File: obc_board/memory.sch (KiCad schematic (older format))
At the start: 10 parts

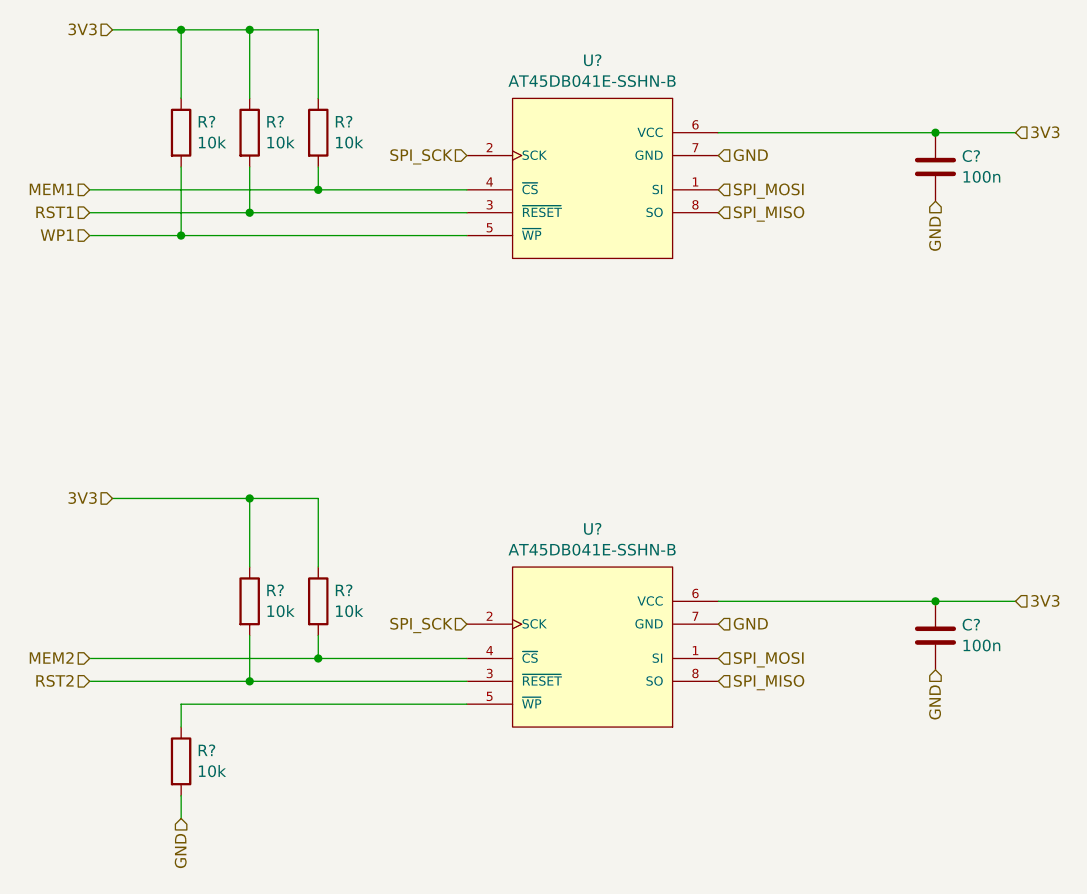
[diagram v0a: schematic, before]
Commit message: updated footprints
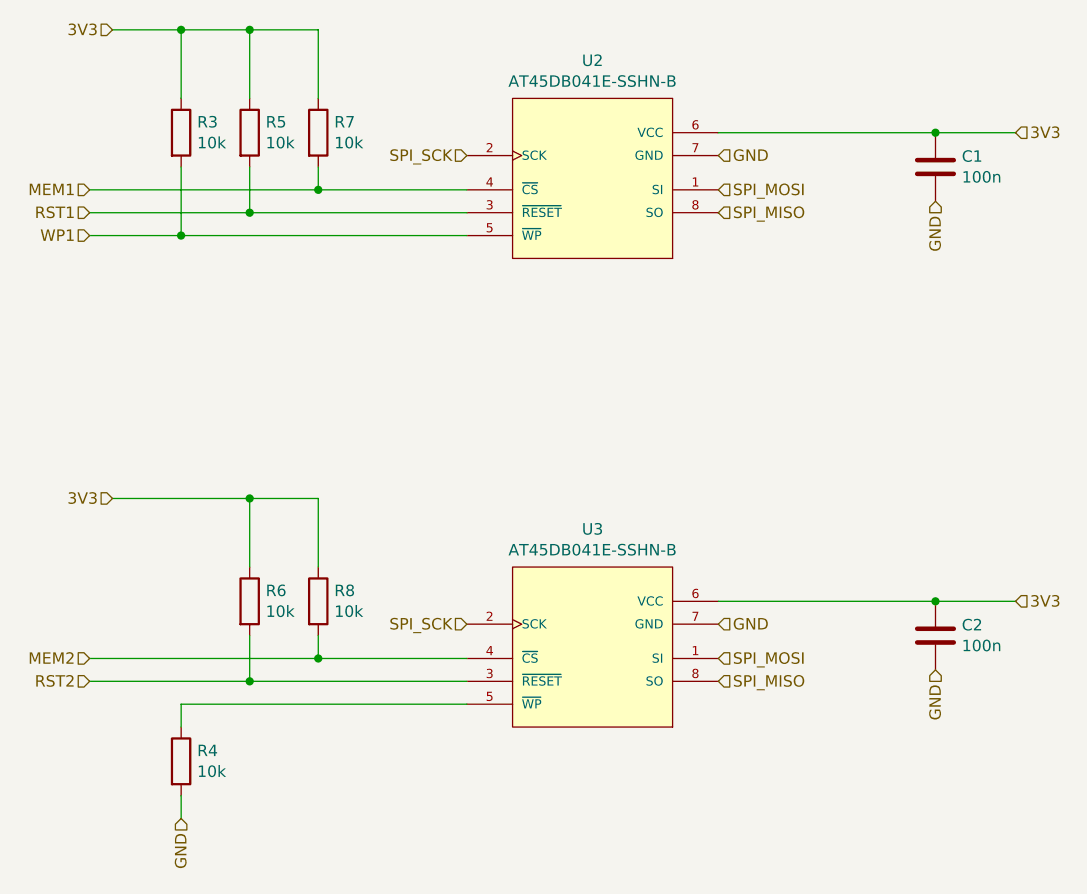
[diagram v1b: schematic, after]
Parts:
- C1, C2: renamed from C?; footprint (none) -> cubesat_obc:CAPC1005X55N; Digikey Part Number (none) -> 490-13342-1-ND
- U2, U3: renamed from U?; footprint SOIC127P600X175-8N -> Package_SO:SOIC-8-N7_3.9x4.9mm_P1.27mm; Digikey Part Number (none) -> 1265-1067-5-ND
- gave numbers to parts that had none: 6
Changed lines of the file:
@@
 P 5200 2950
 AR Path="/5E7EC636/5F3B7CBB" Ref="U?"  Part="1"
-AR Path="/5F3B62A5/5F3B7CBB" Ref="U?"  Part="1"
-F 0 "U?" H 5200 3765 50  0000 C CNN
+AR Path="/5F3B62A5/5F3B7CBB" Ref="U2"  Part="1"
+F 0 "U2" H 5200 3765 50  0000 C CNN
 F 1 "AT45DB041E-SSHN-B" H 5200 3674 50  0000 C CNN
-F 2 "SOIC127P600X175-8N" H 5200 2950 50  0001 L BNN
-F 3 "Adesto Technologies" H 5200 2950 50  0001 L BNN
+F 2 "Package_SO:SOIC-8-N7_3.9x4.9mm_P1.27mm" H 5200 2950 50  0001 L BNN
+F 3 "http://www.adestotech.com/wp-content/uploads/DS-AT45DB041E-HTADD.pdf" H 5200 2950 50  0001 L BNN
+F 4 "1265-1067-5-ND" H 5200 2950 50  0001 C CNN "Digikey Part Number"
 	1    5200 2950
 	1    0    0    -1
@@
 	5750 2450 6700 2450
 $Comp
-L Device:C C?
+L Device:C C1
 U 1 1 5F3B8BBB
 P 6700 2600
-F 0 "C?" H 6815 2646 50  0000 L CNN
+F 0 "C1" H 6815 2646 50  0000 L CNN
 F 1 "100n" H 6815 2555 50  0000 L CNN
-F 2 "" H 6738 2450 50  0001 C CNN
-F 3 "~" H 6700 2600 50  0001 C CNN
+F 2 "cubesat_obc:CAPC1005X55N" H 6738 2450 50  0001 C CNN
+F 3 "https://search.murata.co.jp/Ceramy/image/img/A01X/G101/ENG/GRM155R71H104KE14-01.pdf" H 6700 2600 50  0001 C CNN
+F 4 "	490-13342-1-ND" H 6700 2600 50  0001 C CNN "Digikey Part Number"
 	1    6700 2600
 	1    0    0    -1
@@
 RST1
 $Comp
-L Device:R R?
+L Device:R R7
 U 1 1 5F42F3C4
 P 4000 2450
-F 0 "R?" H 4070 2496 50  0000 L CNN
+F 0 "R7" H 4070 2496 50  0000 L CNN
 F 1 "10k" H 4070 2405 50  0000 L CNN
 F 2 "" V 3930 2450 50  0001 C CNN
@@
 	4000 2700 4650 2700
 $Comp
-L Device:R R?
+L Device:R R5
 U 1 1 5F4303A6
 P 3700 2450
-F 0 "R?" H 3770 2496 50  0000 L CNN
+F 0 "R5" H 3770 2496 50  0000 L CNN
 F 1 "10k" H 3770 2405 50  0000 L CNN
 F 2 "" V 3630 2450 50  0001 C CNN
@@
 $EndComp
 $Comp
-L Device:R R?
+L Device:R R3
 U 1 1 5F430694
 P 3400 2450
-F 0 "R?" H 3470 2496 50  0000 L CNN
+F 0 "R3" H 3470 2496 50  0000 L CNN
 F 1 "10k" H 3470 2405 50  0000 L CNN
 F 2 "" V 3330 2450 50  0001 C CNN
@@
 P 5200 5000
 AR Path="/5E7EC636/5F434A8C" Ref="U?"  Part="1"
-AR Path="/5F3B62A5/5F434A8C" Ref="U?"  Part="1"
-F 0 "U?" H 5200 5815 50  0000 C CNN
+AR Path="/5F3B62A5/5F434A8C" Ref="U3"  Part="1"
+F 0 "U3" H 5200 5815 50  0000 C CNN
 F 1 "AT45DB041E-SSHN-B" H 5200 5724 50  0000 C CNN
-F 2 "SOIC127P600X175-8N" H 5200 5000 50  0001 L BNN
-F 3 "Adesto Technologies" H 5200 5000 50  0001 L BNN
+F 2 "Package_SO:SOIC-8-N7_3.9x4.9mm_P1.27mm" H 5200 5000 50  0001 L BNN
+F 3 "http://www.adestotech.com/wp-content/uploads/DS-AT45DB041E-HTADD.pdf" H 5200 5000 50  0001 L BNN
+F 4 "1265-1067-5-ND" H 5200 5000 50  0001 C CNN "Digikey Part Number"
 	1    5200 5000
 	1    0    0    -1
@@
 	5750 4500 6700 4500
 $Comp
-L Device:C C?
+L Device:C C2
 U 1 1 5F434A98
 P 6700 4650
-F 0 "C?" H 6815 4696 50  0000 L CNN
+F 0 "C2" H 6815 4696 50  0000 L CNN
 F 1 "100n" H 6815 4605 50  0000 L CNN
-F 2 "" H 6738 4500 50  0001 C CNN
-F 3 "~" H 6700 4650 50  0001 C CNN
+F 2 "cubesat_obc:CAPC1005X55N" H 6738 4500 50  0001 C CNN
+F 3 "https://search.murata.co.jp/Ceramy/image/img/A01X/G101/ENG/GRM155R71H104KE14-01.pdf" H 6700 4650 50  0001 C CNN
+F 4 "	490-13342-1-ND" H 6700 4650 50  0001 C CNN "Digikey Part Number"
 	1    6700 4650
 	1    0    0    -1
@@
 RST2
 $Comp
-L Device:R R?
+L Device:R R8
 U 1 1 5F434AA3
 P 4000 4500
-F 0 "R?" H 4070 4546 50  0000 L CNN
+F 0 "R8" H 4070 4546 50  0000 L CNN
 F 1 "10k" H 4070 4455 50  0000 L CNN
 F 2 "" V 3930 4500 50  0001 C CNN
@@
 	4000 4750 4650 4750
 $Comp
-L Device:R R?
+L Device:R R6
 U 1 1 5F434AAD
 P 3700 4500
-F 0 "R?" H 3770 4546 50  0000 L CNN
+F 0 "R6" H 3770 4546 50  0000 L CNN
 F 1 "10k" H 3770 4455 50  0000 L CNN
 F 2 "" V 3630 4500 50  0001 C CNN
@@
 Connection ~ 3400 2900
 $Comp
-L Device:R R?
+L Device:R R4
 U 1 1 5F43582E
 P 3400 5200
-F 0 "R?" H 3470 5246 50  0000 L CNN
+F 0 "R4" H 3470 5246 50  0000 L CNN
 F 1 "10k" H 3470 5155 50  0000 L CNN
 F 2 "" V 3330 5200 50  0001 C CNN

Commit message: footprints
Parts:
- C1, C2: footprint cubesat_obc:CAPC1005X55N -> Capacitor_SMD:C_0402_1005Metric; Digikey Part Number 490-13342-1-ND -> 490-16433-1-ND
- R3, R4, R5, R6, R7, R8: footprint (none) -> Resistor_SMD:R_0402_1005Metric; Digikey Part Number (none) -> 311-10.0KLRCT-ND
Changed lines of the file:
@@
 F 0 "C1" H 6815 2646 50  0000 L CNN
 F 1 "100n" H 6815 2555 50  0000 L CNN
-F 2 "cubesat_obc:CAPC1005X55N" H 6738 2450 50  0001 C CNN
-F 3 "https://search.murata.co.jp/Ceramy/image/img/A01X/G101/ENG/GRM155R71H104KE14-01.pdf" H 6700 2600 50  0001 C CNN
-F 4 "	490-13342-1-ND" H 6700 2600 50  0001 C CNN "Digikey Part Number"
+F 2 "Capacitor_SMD:C_0402_1005Metric" H 6738 2450 50  0001 C CNN
+F 3 "https://search.murata.co.jp/Ceramy/image/img/A01X/G101/ENG/GCM155R71C104JA55-01.pdf" H 6700 2600 50  0001 C CNN
+F 4 "490-16433-1-ND" H 6700 2600 50  0001 C CNN "Digikey Part Number"
 	1    6700 2600
 	1    0    0    -1
@@
 F 0 "R7" H 4070 2496 50  0000 L CNN
 F 1 "10k" H 4070 2405 50  0000 L CNN
-F 2 "" V 3930 2450 50  0001 C CNN
-F 3 "~" H 4000 2450 50  0001 C CNN
+F 2 "Resistor_SMD:R_0402_1005Metric" V 3930 2450 50  0001 C CNN
+F 3 "https://www.yageo.com/upload/media/product/productsearch/datasheet/rchip/PYu-RC_Group_51_RoHS_L_11.pdf~" H 4000 2450 50  0001 C CNN
+F 4 "311-10.0KLRCT-ND" H 4000 2450 50  0001 C CNN "Digikey Part Number"
 	1    4000 2450
 	1    0    0    -1
@@
 F 0 "R5" H 3770 2496 50  0000 L CNN
 F 1 "10k" H 3770 2405 50  0000 L CNN
-F 2 "" V 3630 2450 50  0001 C CNN
-F 3 "~" H 3700 2450 50  0001 C CNN
+F 2 "Resistor_SMD:R_0402_1005Metric" V 3630 2450 50  0001 C CNN
+F 3 "https://www.yageo.com/upload/media/product/productsearch/datasheet/rchip/PYu-RC_Group_51_RoHS_L_11.pdf~" H 3700 2450 50  0001 C CNN
+F 4 "311-10.0KLRCT-ND" H 3700 2450 50  0001 C CNN "Digikey Part Number"
 	1    3700 2450
 	1    0    0    -1
@@
 F 0 "R3" H 3470 2496 50  0000 L CNN
 F 1 "10k" H 3470 2405 50  0000 L CNN
-F 2 "" V 3330 2450 50  0001 C CNN
-F 3 "~" H 3400 2450 50  0001 C CNN
+F 2 "Resistor_SMD:R_0402_1005Metric" V 3330 2450 50  0001 C CNN
+F 3 "https://www.yageo.com/upload/media/product/productsearch/datasheet/rchip/PYu-RC_Group_51_RoHS_L_11.pdf~" H 3400 2450 50  0001 C CNN
+F 4 "311-10.0KLRCT-ND" H 3400 2450 50  0001 C CNN "Digikey Part Number"
 	1    3400 2450
 	1    0    0    -1
@@
 F 0 "C2" H 6815 4696 50  0000 L CNN
 F 1 "100n" H 6815 4605 50  0000 L CNN
-F 2 "cubesat_obc:CAPC1005X55N" H 6738 4500 50  0001 C CNN
-F 3 "https://search.murata.co.jp/Ceramy/image/img/A01X/G101/ENG/GRM155R71H104KE14-01.pdf" H 6700 4650 50  0001 C CNN
-F 4 "	490-13342-1-ND" H 6700 4650 50  0001 C CNN "Digikey Part Number"
+F 2 "Capacitor_SMD:C_0402_1005Metric" H 6738 4500 50  0001 C CNN
+F 3 "https://search.murata.co.jp/Ceramy/image/img/A01X/G101/ENG/GCM155R71C104JA55-01.pdf" H 6700 4650 50  0001 C CNN
+F 4 "490-16433-1-ND" H 6700 4650 50  0001 C CNN "Digikey Part Number"
 	1    6700 4650
 	1    0    0    -1
@@
 F 0 "R8" H 4070 4546 50  0000 L CNN
 F 1 "10k" H 4070 4455 50  0000 L CNN
-F 2 "" V 3930 4500 50  0001 C CNN
-F 3 "~" H 4000 4500 50  0001 C CNN
+F 2 "Resistor_SMD:R_0402_1005Metric" V 3930 4500 50  0001 C CNN
+F 3 "https://www.yageo.com/upload/media/product/productsearch/datasheet/rchip/PYu-RC_Group_51_RoHS_L_11.pdf~" H 4000 4500 50  0001 C CNN
+F 4 "311-10.0KLRCT-ND" H 4000 4500 50  0001 C CNN "Digikey Part Number"
 	1    4000 4500
 	1    0    0    -1
@@
 F 0 "R6" H 3770 4546 50  0000 L CNN
 F 1 "10k" H 3770 4455 50  0000 L CNN
-F 2 "" V 3630 4500 50  0001 C CNN
-F 3 "~" H 3700 4500 50  0001 C CNN
+F 2 "Resistor_SMD:R_0402_1005Metric" V 3630 4500 50  0001 C CNN
+F 3 "https://www.yageo.com/upload/media/product/productsearch/datasheet/rchip/PYu-RC_Group_51_RoHS_L_11.pdf~" H 3700 4500 50  0001 C CNN
+F 4 "311-10.0KLRCT-ND" H 3700 4500 50  0001 C CNN "Digikey Part Number"
 	1    3700 4500
 	1    0    0    -1
@@
 F 0 "R4" H 3470 5246 50  0000 L CNN
 F 1 "10k" H 3470 5155 50  0000 L CNN
-F 2 "" V 3330 5200 50  0001 C CNN
-F 3 "~" H 3400 5200 50  0001 C CNN
+F 2 "Resistor_SMD:R_0402_1005Metric" V 3330 5200 50  0001 C CNN
+F 3 "https://www.yageo.com/upload/media/product/productsearch/datasheet/rchip/PYu-RC_Group_51_RoHS_L_11.pdf~" H 3400 5200 50  0001 C CNN
+F 4 "311-10.0KLRCT-ND" H 3400 5200 50  0001 C CNN "Digikey Part Number"
 	1    3400 5200
 	1    0    0    -1

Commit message: expose more ios
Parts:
- U2, U3: footprint Package_SO:SOIC-8-N7_3.9x4.9mm_P1.27mm -> Package_SO:SOIC-8_3.9x4.9mm_P1.27mm
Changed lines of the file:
@@
 $Descr A4 11693 8268
 encoding utf-8
-Sheet 2 5
+Sheet 2 6
 Title ""
 Date ""
@@
 F 0 "U2" H 5200 3765 50  0000 C CNN
 F 1 "AT45DB041E-SSHN-B" H 5200 3674 50  0000 C CNN
-F 2 "Package_SO:SOIC-8-N7_3.9x4.9mm_P1.27mm" H 5200 2950 50  0001 L BNN
+F 2 "Package_SO:SOIC-8_3.9x4.9mm_P1.27mm" H 5200 2950 50  0001 L BNN
 F 3 "http://www.adestotech.com/wp-content/uploads/DS-AT45DB041E-HTADD.pdf" H 5200 2950 50  0001 L BNN
 F 4 "1265-1067-5-ND" H 5200 2950 50  0001 C CNN "Digikey Part Number"
@@
 F 0 "U3" H 5200 5815 50  0000 C CNN
 F 1 "AT45DB041E-SSHN-B" H 5200 5724 50  0000 C CNN
-F 2 "Package_SO:SOIC-8-N7_3.9x4.9mm_P1.27mm" H 5200 5000 50  0001 L BNN
+F 2 "Package_SO:SOIC-8_3.9x4.9mm_P1.27mm" H 5200 5000 50  0001 L BNN
 F 3 "http://www.adestotech.com/wp-content/uploads/DS-AT45DB041E-HTADD.pdf" H 5200 5000 50  0001 L BNN
 F 4 "1265-1067-5-ND" H 5200 5000 50  0001 C CNN "Digikey Part Number"

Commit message: pcb layout
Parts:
- renumbered U2 to U1, U3 to U2
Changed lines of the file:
@@
 $Descr A4 11693 8268
 encoding utf-8
-Sheet 2 6
+Sheet 2 7
 Title ""
 Date ""
@@
 P 5200 2950
 AR Path="/5E7EC636/5F3B7CBB" Ref="U?"  Part="1"
-AR Path="/5F3B62A5/5F3B7CBB" Ref="U2"  Part="1"
-F 0 "U2" H 5200 3765 50  0000 C CNN
+AR Path="/5F3B62A5/5F3B7CBB" Ref="U1"  Part="1"
+F 0 "U1" H 5200 3765 50  0000 C CNN
 F 1 "AT45DB041E-SSHN-B" H 5200 3674 50  0000 C CNN
 F 2 "Package_SO:SOIC-8_3.9x4.9mm_P1.27mm" H 5200 2950 50  0001 L BNN
@@
 F 1 "10k" H 4070 2405 50  0000 L CNN
 F 2 "Resistor_SMD:R_0402_1005Metric" V 3930 2450 50  0001 C CNN
-F 3 "https://www.yageo.com/upload/media/product/productsearch/datasheet/rchip/PYu-RC_Group_51_RoHS_L_11.pdf~" H 4000 2450 50  0001 C CNN
+F 3 "https://www.yageo.com/upload/media/product/productsearch/datasheet/rchip/PYu-RC_Group_51_RoHS_L_11.pdf" H 4000 2450 50  0001 C CNN
 F 4 "311-10.0KLRCT-ND" H 4000 2450 50  0001 C CNN "Digikey Part Number"
 	1    4000 2450
@@
 F 1 "10k" H 3770 2405 50  0000 L CNN
 F 2 "Resistor_SMD:R_0402_1005Metric" V 3630 2450 50  0001 C CNN
-F 3 "https://www.yageo.com/upload/media/product/productsearch/datasheet/rchip/PYu-RC_Group_51_RoHS_L_11.pdf~" H 3700 2450 50  0001 C CNN
+F 3 "https://www.yageo.com/upload/media/product/productsearch/datasheet/rchip/PYu-RC_Group_51_RoHS_L_11.pdf" H 3700 2450 50  0001 C CNN
 F 4 "311-10.0KLRCT-ND" H 3700 2450 50  0001 C CNN "Digikey Part Number"
 	1    3700 2450
@@
 F 1 "10k" H 3470 2405 50  0000 L CNN
 F 2 "Resistor_SMD:R_0402_1005Metric" V 3330 2450 50  0001 C CNN
-F 3 "https://www.yageo.com/upload/media/product/productsearch/datasheet/rchip/PYu-RC_Group_51_RoHS_L_11.pdf~" H 3400 2450 50  0001 C CNN
+F 3 "https://www.yageo.com/upload/media/product/productsearch/datasheet/rchip/PYu-RC_Group_51_RoHS_L_11.pdf" H 3400 2450 50  0001 C CNN
 F 4 "311-10.0KLRCT-ND" H 3400 2450 50  0001 C CNN "Digikey Part Number"
 	1    3400 2450
@@
 P 5200 5000
 AR Path="/5E7EC636/5F434A8C" Ref="U?"  Part="1"
-AR Path="/5F3B62A5/5F434A8C" Ref="U3"  Part="1"
-F 0 "U3" H 5200 5815 50  0000 C CNN
+AR Path="/5F3B62A5/5F434A8C" Ref="U2"  Part="1"
+F 0 "U2" H 5200 5815 50  0000 C CNN
 F 1 "AT45DB041E-SSHN-B" H 5200 5724 50  0000 C CNN
 F 2 "Package_SO:SOIC-8_3.9x4.9mm_P1.27mm" H 5200 5000 50  0001 L BNN
@@
 F 1 "10k" H 4070 4455 50  0000 L CNN
 F 2 "Resistor_SMD:R_0402_1005Metric" V 3930 4500 50  0001 C CNN
-F 3 "https://www.yageo.com/upload/media/product/productsearch/datasheet/rchip/PYu-RC_Group_51_RoHS_L_11.pdf~" H 4000 4500 50  0001 C CNN
+F 3 "https://www.yageo.com/upload/media/product/productsearch/datasheet/rchip/PYu-RC_Group_51_RoHS_L_11.pdf" H 4000 4500 50  0001 C CNN
 F 4 "311-10.0KLRCT-ND" H 4000 4500 50  0001 C CNN "Digikey Part Number"
 	1    4000 4500
@@
 F 1 "10k" H 3770 4455 50  0000 L CNN
 F 2 "Resistor_SMD:R_0402_1005Metric" V 3630 4500 50  0001 C CNN
-F 3 "https://www.yageo.com/upload/media/product/productsearch/datasheet/rchip/PYu-RC_Group_51_RoHS_L_11.pdf~" H 3700 4500 50  0001 C CNN
+F 3 "https://www.yageo.com/upload/media/product/productsearch/datasheet/rchip/PYu-RC_Group_51_RoHS_L_11.pdf" H 3700 4500 50  0001 C CNN
 F 4 "311-10.0KLRCT-ND" H 3700 4500 50  0001 C CNN "Digikey Part Number"
 	1    3700 4500
@@
 F 1 "10k" H 3470 5155 50  0000 L CNN
 F 2 "Resistor_SMD:R_0402_1005Metric" V 3330 5200 50  0001 C CNN
-F 3 "https://www.yageo.com/upload/media/product/productsearch/datasheet/rchip/PYu-RC_Group_51_RoHS_L_11.pdf~" H 3400 5200 50  0001 C CNN
+F 3 "https://www.yageo.com/upload/media/product/productsearch/datasheet/rchip/PYu-RC_Group_51_RoHS_L_11.pdf" H 3400 5200 50  0001 C CNN
 F 4 "311-10.0KLRCT-ND" H 3400 5200 50  0001 C CNN "Digikey Part Number"
 	1    3400 5200

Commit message: relayout
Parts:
- renumbered C1 to C19, C2 to C20, U1 to U2, U2 to U3
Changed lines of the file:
@@
 P 5200 2950
 AR Path="/5E7EC636/5F3B7CBB" Ref="U?"  Part="1"
-AR Path="/5F3B62A5/5F3B7CBB" Ref="U1"  Part="1"
-F 0 "U1" H 5200 3765 50  0000 C CNN
+AR Path="/5F3B62A5/5F3B7CBB" Ref="U2"  Part="1"
+F 0 "U2" H 5200 3765 50  0000 C CNN
 F 1 "AT45DB041E-SSHN-B" H 5200 3674 50  0000 C CNN
 F 2 "Package_SO:SOIC-8_3.9x4.9mm_P1.27mm" H 5200 2950 50  0001 L BNN
@@
 	5750 2450 6700 2450
 $Comp
-L Device:C C1
+L Device:C C19
 U 1 1 5F3B8BBB
 P 6700 2600
-F 0 "C1" H 6815 2646 50  0000 L CNN
+F 0 "C19" H 6815 2646 50  0000 L CNN
 F 1 "100n" H 6815 2555 50  0000 L CNN
 F 2 "Capacitor_SMD:C_0402_1005Metric" H 6738 2450 50  0001 C CNN
@@
 P 5200 5000
 AR Path="/5E7EC636/5F434A8C" Ref="U?"  Part="1"
-AR Path="/5F3B62A5/5F434A8C" Ref="U2"  Part="1"
-F 0 "U2" H 5200 5815 50  0000 C CNN
+AR Path="/5F3B62A5/5F434A8C" Ref="U3"  Part="1"
+F 0 "U3" H 5200 5815 50  0000 C CNN
 F 1 "AT45DB041E-SSHN-B" H 5200 5724 50  0000 C CNN
 F 2 "Package_SO:SOIC-8_3.9x4.9mm_P1.27mm" H 5200 5000 50  0001 L BNN
@@
 	5750 4500 6700 4500
 $Comp
-L Device:C C2
+L Device:C C20
 U 1 1 5F434A98
 P 6700 4650
-F 0 "C2" H 6815 4696 50  0000 L CNN
+F 0 "C20" H 6815 4696 50  0000 L CNN
 F 1 "100n" H 6815 4605 50  0000 L CNN
 F 2 "Capacitor_SMD:C_0402_1005Metric" H 6738 4500 50  0001 C CNN
